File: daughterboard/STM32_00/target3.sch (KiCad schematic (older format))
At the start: 11 parts, among them U3 STM32F103C8Tx

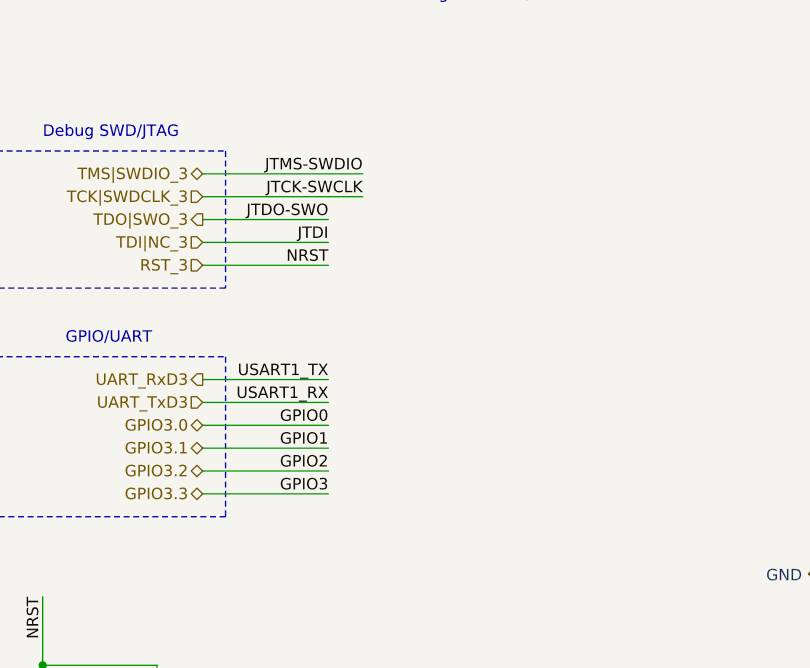
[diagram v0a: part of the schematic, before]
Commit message: added testpoints to daughterboards, updated readme
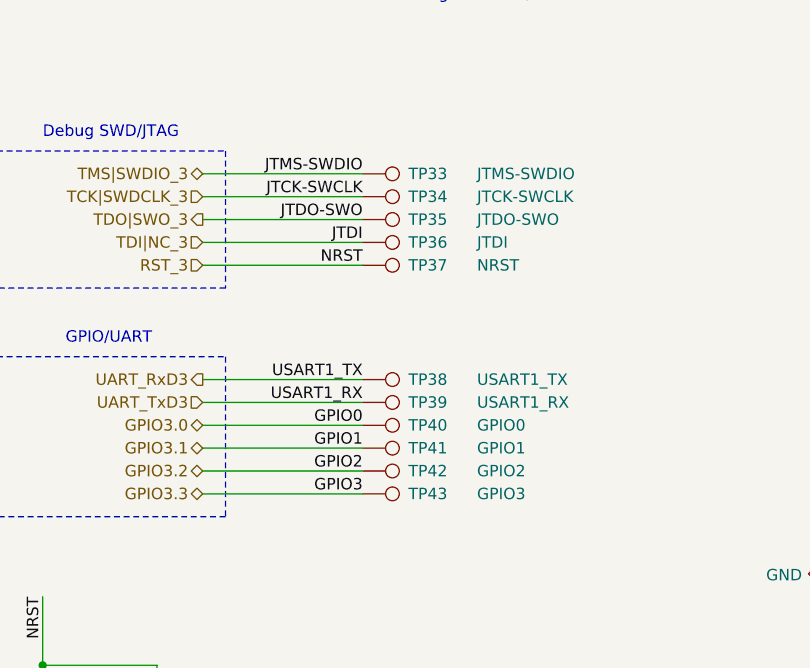
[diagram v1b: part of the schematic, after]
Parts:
- added TP33: JTMS-SWDIO, symbol Connector:TestPoint
- added TP34: JTCK-SWCLK, symbol Connector:TestPoint
- added TP35: JTDO-SWO, symbol Connector:TestPoint
- added TP36: JTDI, symbol Connector:TestPoint
- added TP37: NRST, symbol Connector:TestPoint
- added TP38: USART1_TX, symbol Connector:TestPoint
- added TP39: USART1_RX, symbol Connector:TestPoint
- added TP40: GPIO0, symbol Connector:TestPoint
- added TP41: GPIO1, symbol Connector:TestPoint
- added TP42: GPIO2, symbol Connector:TestPoint
- added TP43: GPIO3, symbol Connector:TestPoint
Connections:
- net GPIO3.0: now also TP40.1
- net GPIO3.1: now also TP41.1
- net GPIO3.2: now also TP42.1
- net GPIO3.3: now also TP43.1
- net RST_3: now also TP37.1
- net TCK|SWDCLK_3: now also TP34.1
- net TDI|NC_3: now also TP36.1
- net TDO|SWO_3: now also TP35.1
- net TMS|SWDIO_3: now also TP33.1
- net UART_RxD3: now also TP38.1
- net UART_TxD3: now also TP39.1
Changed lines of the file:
@@
 JTCK-SWCLK
 Wire Wire Line
-	1650 2700 2200 2700
-Text Label 2200 2700 2    50   ~ 0
+	1650 2700 2350 2700
+Text Label 2350 2700 2    50   ~ 0
 USART1_RX
 Wire Wire Line
-	1650 2600 2200 2600
-Text Label 2200 2600 2    50   ~ 0
+	1650 2600 2350 2600
+Text Label 2350 2600 2    50   ~ 0
 USART1_TX
 Wire Wire Line
-	1650 2100 2200 2100
-Text Label 2200 2100 2    50   ~ 0
+	1650 2100 2350 2100
+Text Label 2350 2100 2    50   ~ 0
 NRST
 Wire Wire Line
-	1650 1900 2200 1900
-Text Label 2200 2000 2    50   ~ 0
+	1650 1900 2350 1900
+Text Label 2350 2000 2    50   ~ 0
 JTDI
 Wire Wire Line
-	2200 2000 1650 2000
-Text Label 2200 1900 2    50   ~ 0
+	2350 2000 1650 2000
+Text Label 2350 1900 2    50   ~ 0
 JTDO-SWO
 Wire Wire Line
-	1650 2800 2200 2800
-Text Label 2200 2800 2    50   ~ 0
+	1650 2800 2350 2800
+Text Label 2350 2800 2    50   ~ 0
 GPIO0
 Wire Wire Line
-	1650 2900 2200 2900
-Text Label 2200 2900 2    50   ~ 0
+	1650 2900 2350 2900
+Text Label 2350 2900 2    50   ~ 0
 GPIO1
 Wire Wire Line
-	1650 3000 2200 3000
-Text Label 2200 3000 2    50   ~ 0
+	1650 3000 2350 3000
+Text Label 2350 3000 2    50   ~ 0
 GPIO2
 Wire Wire Line
-	1650 3100 2200 3100
-Text Label 2200 3100 2    50   ~ 0
+	1650 3100 2350 3100
+Text Label 2350 3100 2    50   ~ 0
 GPIO3
 Text Label 2350 1700 2    50   ~ 0
@@
 Wire Wire Line
 	7200 4250 7050 4250
+$Comp
+L Connector:TestPoint TP?
+U 1 1 619291EA
+P 2350 1700
+AR Path="/616688D6/619291EA" Ref="TP?"  Part="1"
+AR Path="/61668157/619291EA" Ref="TP33"  Part="1"
+F 0 "TP33" V 2350 1900 50  0000 L CNN
+F 1 "JTMS-SWDIO" V 2350 2200 50  0000 L CNN
+F 2 "" H 2550 1700 50  0001 C CNN
+F 3 "~" H 2550 1700 50  0001 C CNN
+	1    2350 1700
+	0    1    1    0
+$EndComp
+$Comp
+L Connector:TestPoint TP?
+U 1 1 619291F0
+P 2350 1800
+AR Path="/616688D6/619291F0" Ref="TP?"  Part="1"
+AR Path="/61668157/619291F0" Ref="TP34"  Part="1"
+F 0 "TP34" V 2350 2000 50  0000 L CNN
+F 1 "JTCK-SWCLK" V 2350 2300 50  0000 L CNN
+F 2 "" H 2550 1800 50  0001 C CNN
+F 3 "~" H 2550 1800 50  0001 C CNN
+	1    2350 1800
+	0    1    1    0
+$EndComp
+$Comp
+L Connector:TestPoint TP?
+U 1 1 619291F6
+P 2350 1900
+AR Path="/616688D6/619291F6" Ref="TP?"  Part="1"
+AR Path="/61668157/619291F6" Ref="TP35"  Part="1"
+F 0 "TP35" V 2350 2100 50  0000 L CNN
+F 1 "JTDO-SWO" V 2350 2400 50  0000 L CNN
+F 2 "" H 2550 1900 50  0001 C CNN
+F 3 "~" H 2550 1900 50  0001 C CNN
+	1    2350 1900
+	0    1    1    0
+$EndComp
+$Comp
+L Connector:TestPoint TP?
+U 1 1 619291FC
+P 2350 2000
+AR Path="/616688D6/619291FC" Ref="TP?"  Part="1"
+AR Path="/61668157/619291FC" Ref="TP36"  Part="1"
+F 0 "TP36" V 2350 2200 50  0000 L CNN
+F 1 "JTDI" V 2350 2500 50  0000 L CNN
+F 2 "" H 2550 2000 50  0001 C CNN
+F 3 "~" H 2550 2000 50  0001 C CNN
+	1    2350 2000
+	0    1    1    0
+$EndComp
+$Comp
+L Connector:TestPoint TP?
+U 1 1 61929202
+P 2350 2100
+AR Path="/616688D6/61929202" Ref="TP?"  Part="1"
+AR Path="/61668157/61929202" Ref="TP37"  Part="1"
+F 0 "TP37" V 2350 2300 50  0000 L CNN
+F 1 "NRST" V 2350 2600 50  0000 L CNN
+F 2 "" H 2550 2100 50  0001 C CNN
+F 3 "~" H 2550 2100 50  0001 C CNN
+	1    2350 2100
+	0    1    1    0
+$EndComp
+$Comp
+L Connector:TestPoint TP?
+U 1 1 61929208
+P 2350 2600
+AR Path="/616688D6/61929208" Ref="TP?"  Part="1"
+AR Path="/61668157/61929208" Ref="TP38"  Part="1"
+F 0 "TP38" V 2350 2800 50  0000 L CNN
+F 1 "USART1_TX" V 2350 3100 50  0000 L CNN
+F 2 "" H 2550 2600 50  0001 C CNN
+F 3 "~" H 2550 2600 50  0001 C CNN
+	1    2350 2600
+	0    1    1    0
+$EndComp
+$Comp
+L Connector:TestPoint TP?
+U 1 1 6192920E
+P 2350 2700
+AR Path="/616688D6/6192920E" Ref="TP?"  Part="1"
+AR Path="/61668157/6192920E" Ref="TP39"  Part="1"
+F 0 "TP39" V 2350 2900 50  0000 L CNN
+F 1 "USART1_RX" V 2350 3200 50  0000 L CNN
+F 2 "" H 2550 2700 50  0001 C CNN
+F 3 "~" H 2550 2700 50  0001 C CNN
+	1    2350 2700
+	0    1    1    0
+$EndComp
+$Comp
+L Connector:TestPoint TP?
+U 1 1 61929214
+P 2350 2800
+AR Path="/616688D6/61929214" Ref="TP?"  Part="1"
+AR Path="/61668157/61929214" Ref="TP40"  Part="1"
+F 0 "TP40" V 2350 3000 50  0000 L CNN
+F 1 "GPIO0" V 2350 3300 50  0000 L CNN
+F 2 "" H 2550 2800 50  0001 C CNN
+F 3 "~" H 2550 2800 50  0001 C CNN
+	1    2350 2800
+	0    1    1    0
+$EndComp
+$Comp
+L Connector:TestPoint TP?
+U 1 1 6192921A
+P 2350 2900
+AR Path="/616688D6/6192921A" Ref="TP?"  Part="1"
+AR Path="/61668157/6192921A" Ref="TP41"  Part="1"
+F 0 "TP41" V 2350 3100 50  0000 L CNN
+F 1 "GPIO1" V 2350 3400 50  0000 L CNN
+F 2 "" H 2550 2900 50  0001 C CNN
+F 3 "~" H 2550 2900 50  0001 C CNN
+	1    2350 2900
+	0    1    1    0
+$EndComp
+$Comp
+L Connector:TestPoint TP?
+U 1 1 61929220
+P 2350 3000
+AR Path="/616688D6/61929220" Ref="TP?"  Part="1"
+AR Path="/61668157/61929220" Ref="TP42"  Part="1"
+F 0 "TP42" V 2350 3200 50  0000 L CNN
+F 1 "GPIO2" V 2350 3500 50  0000 L CNN
+F 2 "" H 2550 3000 50  0001 C CNN
+F 3 "~" H 2550 3000 50  0001 C CNN
+	1    2350 3000
+	0    1    1    0
+$EndComp
+$Comp
+L Connector:TestPoint TP?
+U 1 1 61929226
+P 2350 3100
+AR Path="/616688D6/61929226" Ref="TP?"  Part="1"
+AR Path="/61668157/61929226" Ref="TP43"  Part="1"
+F 0 "TP43" V 2350 3300 50  0000 L CNN
+F 1 "GPIO3" V 2350 3600 50  0000 L CNN
+F 2 "" H 2550 3100 50  0001 C CNN
+F 3 "~" H 2550 3100 50  0001 C CNN
+	1    2350 3100
+	0    1    1    0
+$EndComp
 $EndSCHEMATC

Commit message: finished layout of STM32 daughterboard
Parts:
- removed C24: 100n, symbol Device:C_Small
- removed TP37: NRST, symbol Connector:TestPoint
- removed TP40: GPIO0, symbol Connector:TestPoint
- removed TP41: GPIO1, symbol Connector:TestPoint
- removed TP42: GPIO2, symbol Connector:TestPoint
- removed TP43: GPIO3, symbol Connector:TestPoint
- C18, C19, C20, C21, C22, C23: footprint (none) -> Capacitor_SMD:C_0603_1608Metric_Pad1.05x0.95mm_HandSolder
- JP6, JP7: footprint (none) -> Jumper:SolderJumper-2_P1.3mm_Open_TrianglePad1.0x1.5mm
- R5: footprint (none) -> Resistor_SMD:R_0603_1608Metric_Pad1.05x0.95mm_HandSolder
- TP33, TP34, TP35, TP36, TP38, TP39: footprint (none) -> TestPoint:TestPoint_Pad_1.0x1.0mm
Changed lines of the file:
@@
 F 0 "C20" H 7892 1846 50  0000 L CNN
 F 1 "100n" H 7892 1755 50  0000 L CNN
-F 2 "" H 7800 1800 50  0001 C CNN
+F 2 "Capacitor_SMD:C_0603_1608Metric_Pad1.05x0.95mm_HandSolder" H 7800 1800 50  0001 C CNN
 F 3 "~" H 7800 1800 50  0001 C CNN
 	1    7800 1800
@@
 F 0 "C21" H 8392 1846 50  0000 L CNN
 F 1 "100n" H 8392 1755 50  0000 L CNN
-F 2 "" H 8300 1800 50  0001 C CNN
+F 2 "Capacitor_SMD:C_0603_1608Metric_Pad1.05x0.95mm_HandSolder" H 8300 1800 50  0001 C CNN
 F 3 "~" H 8300 1800 50  0001 C CNN
 	1    8300 1800
@@
 F 0 "C22" H 8842 1846 50  0000 L CNN
 F 1 "100n" H 8842 1755 50  0000 L CNN
-F 2 "" H 8750 1800 50  0001 C CNN
+F 2 "Capacitor_SMD:C_0603_1608Metric_Pad1.05x0.95mm_HandSolder" H 8750 1800 50  0001 C CNN
 F 3 "~" H 8750 1800 50  0001 C CNN
 	1    8750 1800
-	1    0    0    -1
-$EndComp
-$Comp
-L Device:C_Small C?
-U 1 1 6194EAD8
-P 9650 1800
-AR Path="/616688D6/6194EAD8" Ref="C?"  Part="1"
-AR Path="/61668157/6194EAD8" Ref="C24"  Part="1"
-F 0 "C24" H 9742 1846 50  0000 L CNN
-F 1 "100n" H 9742 1755 50  0000 L CNN
-F 2 "" H 9650 1800 50  0001 C CNN
-F 3 "~" H 9650 1800 50  0001 C CNN
-	1    9650 1800
 	1    0    0    -1
 $EndComp
@@
 F 0 "C19" H 7392 1846 50  0000 L CNN
 F 1 "4.7u" H 7392 1755 50  0000 L CNN
-F 2 "" H 7300 1800 50  0001 C CNN
+F 2 "Capacitor_SMD:C_0603_1608Metric_Pad1.05x0.95mm_HandSolder" H 7300 1800 50  0001 C CNN
 F 3 "~" H 7300 1800 50  0001 C CNN
 	1    7300 1800
@@
 $EndComp
 Wire Wire Line
-	9650 1700 9650 1550
-Wire Wire Line
 	7300 1700 7300 1550
 Connection ~ 7300 1550
@@
 Wire Wire Line
 	8300 1550 8750 1550
-Wire Wire Line
-	9200 1550 9650 1550
 $Comp
 L power:GND #PWR?
 U 1 1 6194EAF2
-P 9650 2100
+P 9200 2100
 AR Path="/616688D6/6194EAF2" Ref="#PWR?"  Part="1"
 AR Path="/61668157/6194EAF2" Ref="#PWR0142"  Part="1"
-F 0 "#PWR0142" H 9650 1850 50  0001 C CNN
-F 1 "GND" H 9655 1927 50  0000 C CNN
-F 2 "" H 9650 2100 50  0001 C CNN
-F 3 "" H 9650 2100 50  0001 C CNN
-	1    9650 2100
-	1    0    0    -1
-$EndComp
-Wire Wire Line
-	9650 2100 9650 2000
-Wire Wire Line
-	9650 2000 9200 2000
+F 0 "#PWR0142" H 9200 1850 50  0001 C CNN
+F 1 "GND" H 9205 1927 50  0000 C CNN
+F 2 "" H 9200 2100 50  0001 C CNN
+F 3 "" H 9200 2100 50  0001 C CNN
+	1    9200 2100
+	1    0    0    -1
+$EndComp
+Wire Wire Line
+	9200 2100 9200 2000
 Wire Wire Line
 	7300 2000 7300 1900
@@
 Wire Wire Line
 	8750 2000 8300 2000
-Wire Wire Line
-	9650 1900 9650 2000
-Connection ~ 9650 2000
 $Comp
 L power:+3V3 #PWR?
 U 1 1 6194EB06
-P 9650 1400
+P 9200 1400
 AR Path="/616688D6/6194EB06" Ref="#PWR?"  Part="1"
 AR Path="/61668157/6194EB06" Ref="#PWR0143"  Part="1"
-F 0 "#PWR0143" H 9650 1250 50  0001 C CNN
-F 1 "+3V3" H 9665 1573 50  0000 C CNN
-F 2 "" H 9650 1400 50  0001 C CNN
-F 3 "" H 9650 1400 50  0001 C CNN
-	1    9650 1400
-	1    0    0    -1
-$EndComp
-Wire Wire Line
-	9650 1400 9650 1550
-Connection ~ 9650 1550
+F 0 "#PWR0143" H 9200 1250 50  0001 C CNN
+F 1 "+3V3" H 9215 1573 50  0000 C CNN
+F 2 "" H 9200 1400 50  0001 C CNN
+F 3 "" H 9200 1400 50  0001 C CNN
+	1    9200 1400
+	1    0    0    -1
+$EndComp
+Wire Wire Line
+	9200 1400 9200 1550
 $Comp
 L Device:C_Small C?
@@
 F 0 "C23" H 9292 1846 50  0000 L CNN
 F 1 "100n" H 9292 1755 50  0000 L CNN
-F 2 "" H 9200 1800 50  0001 C CNN
+F 2 "Capacitor_SMD:C_0603_1608Metric_Pad1.05x0.95mm_HandSolder" H 9200 1800 50  0001 C CNN
 F 3 "~" H 9200 1800 50  0001 C CNN
 	1    9200 1800
@@
 F 0 "R5" V 5596 2150 50  0000 C CNN
 F 1 "100k" V 5505 2150 50  0000 C CNN
-F 2 "" H 5400 2150 50  0001 C CNN
+F 2 "Resistor_SMD:R_0603_1608Metric_Pad1.05x0.95mm_HandSolder" H 5400 2150 50  0001 C CNN
 F 3 "~" H 5400 2150 50  0001 C CNN
 	1    5400 2150
@@
 F 0 "C18" H 1042 4246 50  0000 L CNN
 F 1 "100n" H 1042 4155 50  0000 L CNN
-F 2 "" H 950 4200 50  0001 C CNN
+F 2 "Capacitor_SMD:C_0603_1608Metric_Pad1.05x0.95mm_HandSolder" H 950 4200 50  0001 C CNN
 F 3 "~" H 950 4200 50  0001 C CNN
 	1    950  4200
@@
 F 0 "JP6" V 1496 4112 50  0000 R CNN
 F 1 "NRST3" V 1405 4112 50  0000 R CNN
-F 2 "" H 1450 4200 50  0001 C CNN
+F 2 "Jumper:SolderJumper-2_P1.3mm_Open_TrianglePad1.0x1.5mm" H 1450 4200 50  0001 C CNN
 F 3 "~" H 1450 4200 50  0001 C CNN
 	1    1450 4200
@@
 F 0 "JP7" H 4750 3655 50  0000 C CNN
 F 1 "NJRST3" H 4750 3564 50  0000 C CNN
-F 2 "" H 4750 3450 50  0001 C CNN
+F 2 "Jumper:SolderJumper-2_P1.3mm_Open_TrianglePad1.0x1.5mm" H 4750 3450 50  0001 C CNN
 F 3 "~" H 4750 3450 50  0001 C CNN
 	1    4750 3450
@@
 F 0 "TP33" V 2350 1900 50  0000 L CNN
 F 1 "JTMS-SWDIO" V 2350 2200 50  0000 L CNN
-F 2 "" H 2550 1700 50  0001 C CNN
+F 2 "TestPoint:TestPoint_Pad_1.0x1.0mm" H 2550 1700 50  0001 C CNN
 F 3 "~" H 2550 1700 50  0001 C CNN
 	1    2350 1700
@@
 F 0 "TP34" V 2350 2000 50  0000 L CNN
 F 1 "JTCK-SWCLK" V 2350 2300 50  0000 L CNN
-F 2 "" H 2550 1800 50  0001 C CNN
+F 2 "TestPoint:TestPoint_Pad_1.0x1.0mm" H 2550 1800 50  0001 C CNN
 F 3 "~" H 2550 1800 50  0001 C CNN
 	1    2350 1800
@@
 F 0 "TP35" V 2350 2100 50  0000 L CNN
 F 1 "JTDO-SWO" V 2350 2400 50  0000 L CNN
-F 2 "" H 2550 1900 50  0001 C CNN
+F 2 "TestPoint:TestPoint_Pad_1.0x1.0mm" H 2550 1900 50  0001 C CNN
 F 3 "~" H 2550 1900 50  0001 C CNN
 	1    2350 1900
@@
 F 0 "TP36" V 2350 2200 50  0000 L CNN
 F 1 "JTDI" V 2350 2500 50  0000 L CNN
-F 2 "" H 2550 2000 50  0001 C CNN
+F 2 "TestPoint:TestPoint_Pad_1.0x1.0mm" H 2550 2000 50  0001 C CNN
 F 3 "~" H 2550 2000 50  0001 C CNN
 	1    2350 2000
-	0    1    1    0
-$EndComp
-$Comp
-L Connector:TestPoint TP?
-U 1 1 61929202
-P 2350 2100
-AR Path="/616688D6/61929202" Ref="TP?"  Part="1"
-AR Path="/61668157/61929202" Ref="TP37"  Part="1"
-F 0 "TP37" V 2350 2300 50  0000 L CNN
-F 1 "NRST" V 2350 2600 50  0000 L CNN
-F 2 "" H 2550 2100 50  0001 C CNN
-F 3 "~" H 2550 2100 50  0001 C CNN
-	1    2350 2100
 	0    1    1    0
 $EndComp
@@
 F 0 "TP38" V 2350 2800 50  0000 L CNN
 F 1 "USART1_TX" V 2350 3100 50  0000 L CNN
-F 2 "" H 2550 2600 50  0001 C CNN
+F 2 "TestPoint:TestPoint_Pad_1.0x1.0mm" H 2550 2600 50  0001 C CNN
 F 3 "~" H 2550 2600 50  0001 C CNN
 	1    2350 2600
@@
 F 0 "TP39" V 2350 2900 50  0000 L CNN
 F 1 "USART1_RX" V 2350 3200 50  0000 L CNN
-F 2 "" H 2550 2700 50  0001 C CNN
+F 2 "TestPoint:TestPoint_Pad_1.0x1.0mm" H 2550 2700 50  0001 C CNN
 F 3 "~" H 2550 2700 50  0001 C CNN
 	1    2350 2700
 	0    1    1    0
 $EndComp
-$Comp
-L Connector:TestPoint TP?
-U 1 1 61929214
-P 2350 2800
-AR Path="/616688D6/61929214" Ref="TP?"  Part="1"
-AR Path="/61668157/61929214" Ref="TP40"  Part="1"
-F 0 "TP40" V 2350 3000 50  0000 L CNN
-F 1 "GPIO0" V 2350 3300 50  0000 L CNN
-F 2 "" H 2550 2800 50  0001 C CNN
-F 3 "~" H 2550 2800 50  0001 C CNN
-	1    2350 2800
-	0    1    1    0
-$EndComp
-$Comp
-L Connector:TestPoint TP?
-U 1 1 6192921A
-P 2350 2900
-AR Path="/616688D6/6192921A" Ref="TP?"  Part="1"
-AR Path="/61668157/6192921A" Ref="TP41"  Part="1"
-F 0 "TP41" V 2350 3100 50  0000 L CNN
-F 1 "GPIO1" V 2350 3400 50  0000 L CNN
-F 2 "" H 2550 2900 50  0001 C CNN
-F 3 "~" H 2550 2900 50  0001 C CNN
-	1    2350 2900
-	0    1    1    0
-$EndComp
-$Comp
-L Connector:TestPoint TP?
-U 1 1 61929220
-P 2350 3000
-AR Path="/616688D6/61929220" Ref="TP?"  Part="1"
-AR Path="/61668157/61929220" Ref="TP42"  Part="1"
-F 0 "TP42" V 2350 3200 50  0000 L CNN
-F 1 "GPIO2" V 2350 3500 50  0000 L CNN
-F 2 "" H 2550 3000 50  0001 C CNN
-F 3 "~" H 2550 3000 50  0001 C CNN
-	1    2350 3000
-	0    1    1    0
-$EndComp
-$Comp
-L Connector:TestPoint TP?
-U 1 1 61929226
-P 2350 3100
-AR Path="/616688D6/61929226" Ref="TP?"  Part="1"
-AR Path="/61668157/61929226" Ref="TP43"  Part="1"
-F 0 "TP43" V 2350 3300 50  0000 L CNN
-F 1 "GPIO3" V 2350 3600 50  0000 L CNN
-F 2 "" H 2550 3100 50  0001 C CNN
-F 3 "~" H 2550 3100 50  0001 C CNN
-	1    2350 3100
-	0    1    1    0
-$EndComp
